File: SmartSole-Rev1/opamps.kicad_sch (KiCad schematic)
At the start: 23 parts, among them U1 MCP6004

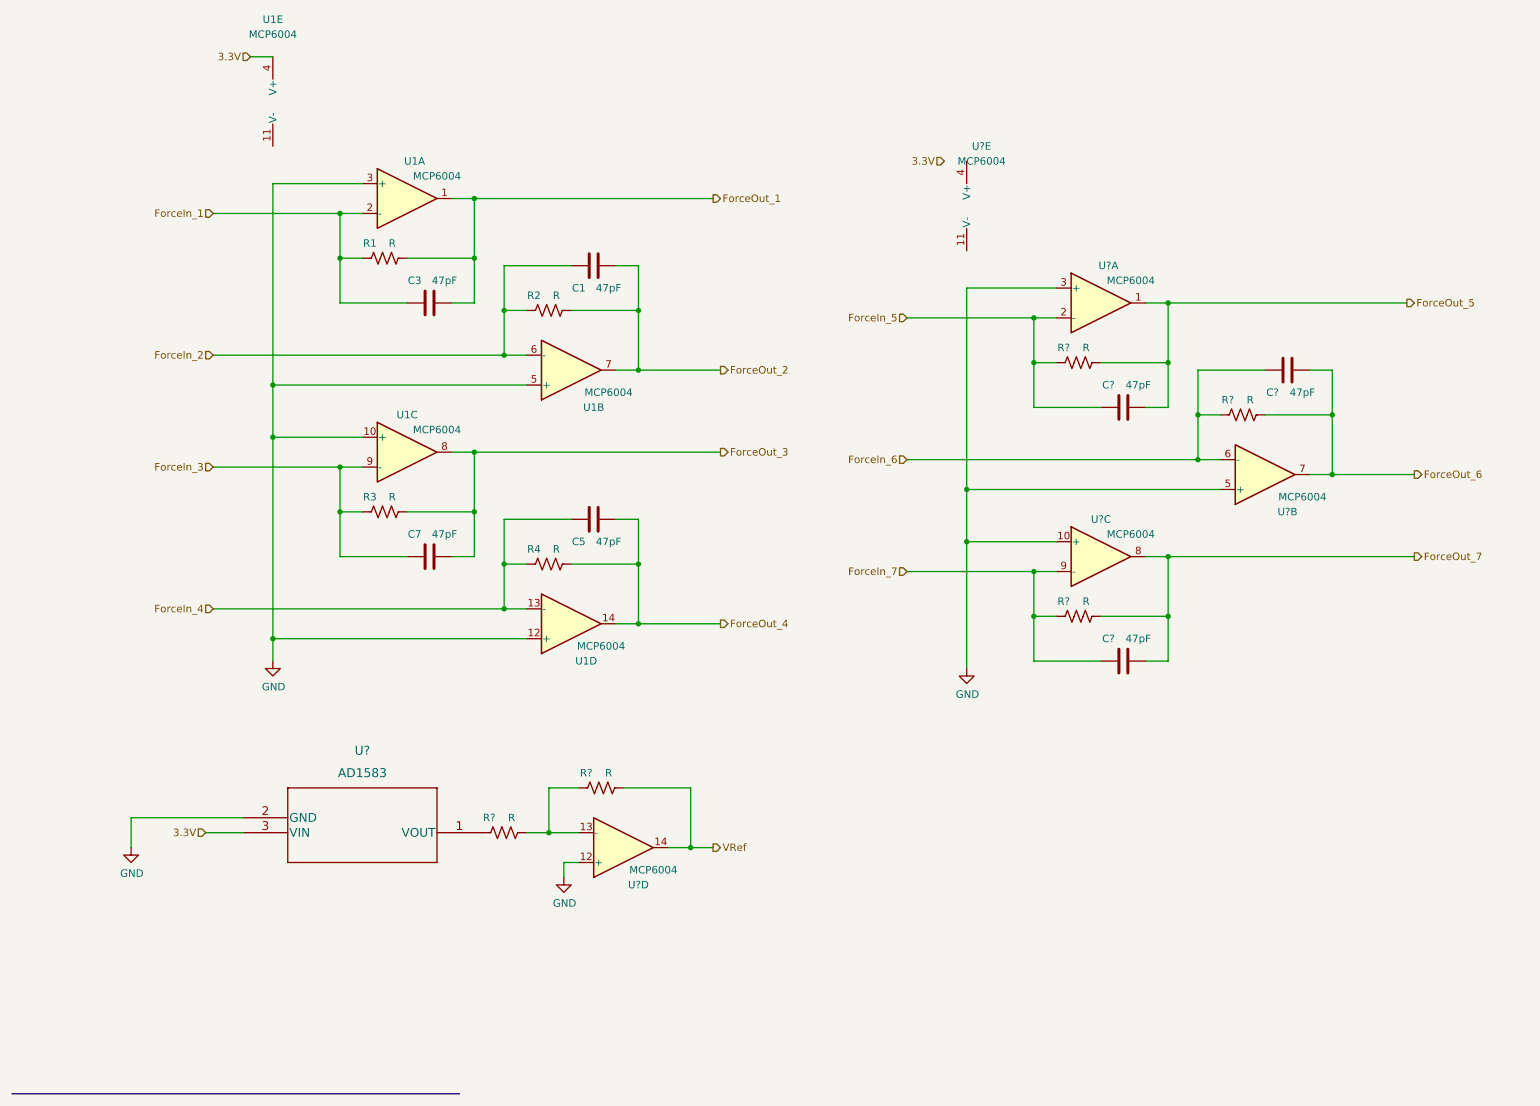
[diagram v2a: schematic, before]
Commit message: Created prelimary board layout, no finalized traces
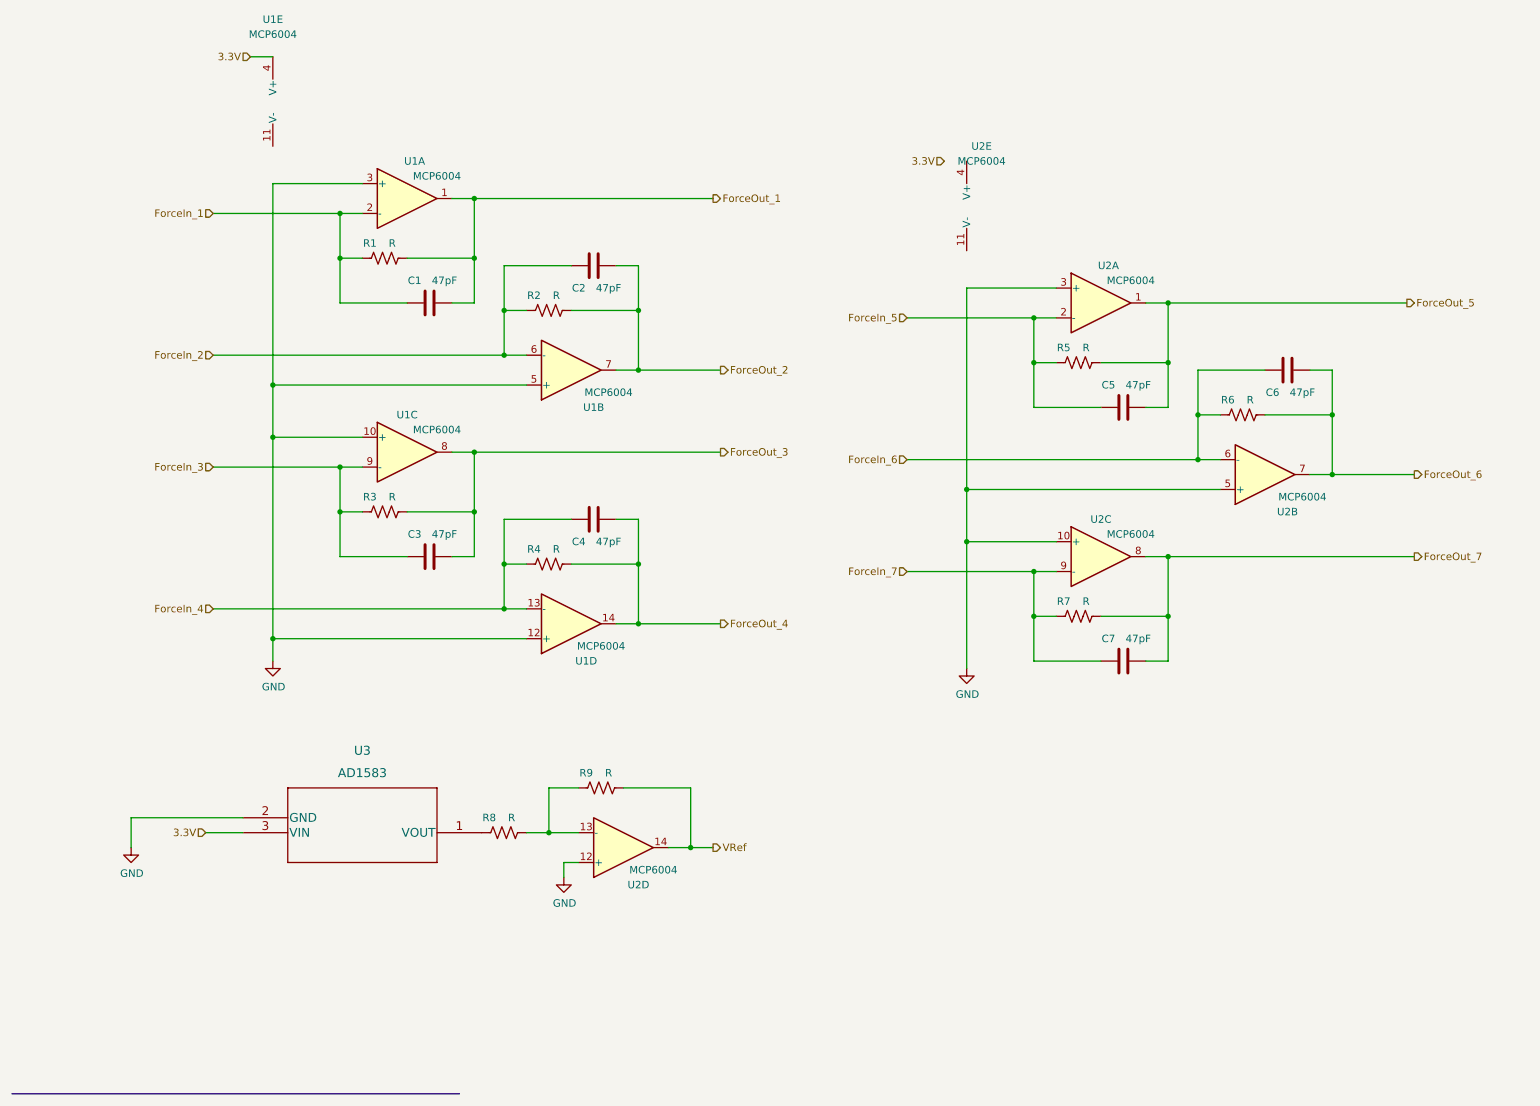
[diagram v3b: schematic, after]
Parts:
- gave numbers to parts that had none: 10
- renumbered C3 to C1, C1 to C2, C7 to C3, C5 to C4
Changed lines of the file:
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@@
   (symbol (lib_id "power:GND") (at 181.61 127 0) (unit 1)
     (in_bom yes) (on_board yes)
-    (property "Reference" "#PWR?" (id 0) (at 181.61 133.35 0)
+    (property "Reference" "#PWR03" (id 0) (at 181.61 133.35 0)
       (effects (font (size 1.27 1.27)) hide)
     )
@@
   (symbol (lib_id "Amplifier_Operational:MCP6004") (at 123.19 157.48 0) (mirror x) (unit 4)
     (in_bom yes) (on_board yes)
-    (property "Reference" "U?" (id 0) (at 125.73 163.83 0))
+    (property "Reference" "U2" (id 0) (at 125.73 163.83 0))
     (property "Value" "MCP6004" (id 1) (at 128.27 161.29 0))
     (property "Footprint" "Package_DIP:DIP-14_W7.62mm" (id 2) (at 121.92 160.02 0)
@@
   (symbol (lib_id "Device:C") (at 90.17 107.95 270) (unit 1)
     (in_bom yes) (on_board yes)
-    (property "Reference" "C7" (id 0) (at 87.63 104.14 90))
+    (property "Reference" "C3" (id 0) (at 87.63 104.14 90))
     (property "Value" "47pF" (id 1) (at 92.71 104.14 90))
     (property "Footprint" "Capacitor_SMD:C_0603_1608Metric" (id 2) (at 86.36 108.9152 0)
@@
   (symbol (lib_id "Device:C") (at 90.17 64.77 270) (unit 1)
     (in_bom yes) (on_board yes)
-    (property "Reference" "C3" (id 0) (at 87.63 60.96 90))
+    (property "Reference" "C1" (id 0) (at 87.63 60.96 90))
     (property "Value" "47pF" (id 1) (at 92.71 60.96 90))
     (property "Footprint" "Capacitor_SMD:C_0603_1608Metric" (id 2) (at 86.36 65.7352 0)
@@
   (symbol (lib_id "Amplifier_Operational:MCP6004") (at 204.47 107.95 0) (unit 3)
     (in_bom yes) (on_board yes)
-    (property "Reference" "U?" (id 0) (at 204.47 101.6 0))
+    (property "Reference" "U2" (id 0) (at 204.47 101.6 0))
     (property "Value" "MCP6004" (id 1) (at 209.55 104.14 0))
     (property "Footprint" "Package_DIP:DIP-14_W7.62mm" (id 2) (at 203.2 105.41 0)
@@
   (symbol (lib_id "Device:C") (at 208.28 82.55 270) (unit 1)
     (in_bom yes) (on_board yes)
-    (property "Reference" "C?" (id 0) (at 205.74 78.74 90))
+    (property "Reference" "C5" (id 0) (at 205.74 78.74 90))
     (property "Value" "47pF" (id 1) (at 210.82 78.74 90))
     (property "Footprint" "Capacitor_SMD:C_0603_1608Metric" (id 2) (at 204.47 83.5152 0)
@@
   (symbol (lib_id "Amplifier_Operational:MCP6004") (at 232.41 93.98 0) (mirror x) (unit 2)
     (in_bom yes) (on_board yes)
-    (property "Reference" "U?" (id 0) (at 236.22 100.33 0))
+    (property "Reference" "U2" (id 0) (at 236.22 100.33 0))
     (property "Value" "MCP6004" (id 1) (at 238.76 97.79 0))
     (property "Footprint" "Package_DIP:DIP-14_W7.62mm" (id 2) (at 231.14 96.52 0)
@@
   (symbol (lib_id "Device:R_US") (at 228.6 83.82 90) (unit 1)
     (in_bom yes) (on_board yes)
-    (property "Reference" "R?" (id 0) (at 226.06 81.28 90))
+    (property "Reference" "R6" (id 0) (at 226.06 81.28 90))
     (property "Value" "R" (id 1) (at 229.87 81.28 90))
     (property "Footprint" "Resistor_SMD:R_0603_1608Metric" (id 2) (at 228.854 82.804 90)
@@
   (symbol (lib_id "Device:R_US") (at 119.38 147.32 90) (unit 1)
     (in_bom yes) (on_board yes)
-    (property "Reference" "R?" (id 0) (at 116.84 144.78 90))
+    (property "Reference" "R9" (id 0) (at 116.84 144.78 90))
     (property "Value" "R" (id 1) (at 120.65 144.78 90))
     (property "Footprint" "Resistor_SMD:R_0603_1608Metric" (id 2) (at 119.634 146.304 90)
@@
   (symbol (lib_id "Device:R_US") (at 200.66 74.93 90) (unit 1)
     (in_bom yes) (on_board yes)
-    (property "Reference" "R?" (id 0) (at 198.12 72.39 90))
+    (property "Reference" "R5" (id 0) (at 198.12 72.39 90))
     (property "Value" "R" (id 1) (at 201.93 72.39 90))
     (property "Footprint" "Resistor_SMD:R_0603_1608Metric" (id 2) (at 200.914 73.914 90)
@@
   (symbol (lib_id "power:GND") (at 39.37 157.48 0) (unit 1)
     (in_bom yes) (on_board yes)
-    (property "Reference" "#PWR?" (id 0) (at 39.37 163.83 0)
+    (property "Reference" "#PWR04" (id 0) (at 39.37 163.83 0)
       (effects (font (size 1.27 1.27)) hide)
     )
@@
   (symbol (lib_id "Device:R_US") (at 200.66 118.11 90) (unit 1)
     (in_bom yes) (on_board yes)
-    (property "Reference" "R?" (id 0) (at 198.12 115.57 90))
+    (property "Reference" "R7" (id 0) (at 198.12 115.57 90))
     (property "Value" "R" (id 1) (at 201.93 115.57 90))
     (property "Footprint" "Resistor_SMD:R_0603_1608Metric" (id 2) (at 200.914 117.094 90)
@@
   (symbol (lib_id "Amplifier_Operational:MCP6004") (at 204.47 64.77 0) (unit 1)
     (in_bom yes) (on_board yes)
-    (property "Reference" "U?" (id 0) (at 205.74 58.42 0))
+    (property "Reference" "U2" (id 0) (at 205.74 58.42 0))
     (property "Value" "MCP6004" (id 1) (at 209.55 60.96 0))
     (property "Footprint" "Package_DIP:DIP-14_W7.62mm" (id 2) (at 203.2 62.23 0)
@@
   (symbol (lib_id "Device:C") (at 118.11 101.6 270) (mirror x) (unit 1)
     (in_bom yes) (on_board yes)
-    (property "Reference" "C5" (id 0) (at 115.57 105.41 90))
+    (property "Reference" "C4" (id 0) (at 115.57 105.41 90))
     (property "Value" "47pF" (id 1) (at 120.65 105.41 90))
     (property "Footprint" "Capacitor_SMD:C_0603_1608Metric" (id 2) (at 114.3 100.6348 0)
@@
   (symbol (lib_id "Device:C") (at 118.11 58.42 270) (mirror x) (unit 1)
     (in_bom yes) (on_board yes)
-    (property "Reference" "C1" (id 0) (at 115.57 62.23 90))
+    (property "Reference" "C2" (id 0) (at 115.57 62.23 90))
     (property "Value" "47pF" (id 1) (at 120.65 62.23 90))
     (property "Footprint" "Capacitor_SMD:C_0603_1608Metric" (id 2) (at 114.3 57.4548 0)
@@
   (symbol (lib_id "Amplifier_Operational:MCP6004") (at 184.15 48.26 0) (unit 5)
     (in_bom yes) (on_board yes) (fields_autoplaced)
-    (property "Reference" "U?" (id 0) (at 184.15 38.1 0))
+    (property "Reference" "U2" (id 0) (at 184.15 38.1 0))
     (property "Value" "MCP6004" (id 1) (at 184.15 40.64 0))
     (property "Footprint" "Package_DIP:DIP-14_W7.62mm" (id 2) (at 182.88 45.72 0)
@@
   (symbol (lib_id "Device:C") (at 236.22 76.2 270) (mirror x) (unit 1)
     (in_bom yes) (on_board yes)
-    (property "Reference" "C?" (id 0) (at 233.68 80.01 90))
+    (property "Reference" "C6" (id 0) (at 233.68 80.01 90))
     (property "Value" "47pF" (id 1) (at 238.76 80.01 90))
     (property "Footprint" "Capacitor_SMD:C_0603_1608Metric" (id 2) (at 232.41 75.2348 0)
@@
   (symbol (lib_id "power:GND") (at 113.03 162.56 0) (unit 1)
     (in_bom yes) (on_board yes)
-    (property "Reference" "#PWR?" (id 0) (at 113.03 168.91 0)
+    (property "Reference" "#PWR05" (id 0) (at 113.03 168.91 0)
       (effects (font (size 1.27 1.27)) hide)
     )
@@
   (symbol (lib_id "CapstoneLibrary:AD1583") (at 99.06 154.94 180) (unit 1)
     (in_bom yes) (on_board yes) (fields_autoplaced)
-    (property "Reference" "U?" (id 0) (at 78.74 140.97 0)
+    (property "Reference" "U3" (id 0) (at 78.74 140.97 0)
       (effects (font (size 1.524 1.524)))
     )
@@
   (symbol (lib_id "Device:C") (at 208.28 125.73 270) (unit 1)
     (in_bom yes) (on_board yes)
-    (property "Reference" "C?" (id 0) (at 205.74 121.92 90))
+    (property "Reference" "C7" (id 0) (at 205.74 121.92 90))
     (property "Value" "47pF" (id 1) (at 210.82 121.92 90))
     (property "Footprint" "Capacitor_SMD:C_0603_1608Metric" (id 2) (at 204.47 126.6952 0)
@@
   (symbol (lib_id "Device:R_US") (at 102.87 154.94 90) (unit 1)
     (in_bom yes) (on_board yes)
-    (property "Reference" "R?" (id 0) (at 100.33 152.4 90))
+    (property "Reference" "R8" (id 0) (at 100.33 152.4 90))
     (property "Value" "R" (id 1) (at 104.14 152.4 90))
     (property "Footprint" "Resistor_SMD:R_0603_1608Metric" (id 2) (at 103.124 153.924 90)

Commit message: First review with rachel, made notes on changes to be made
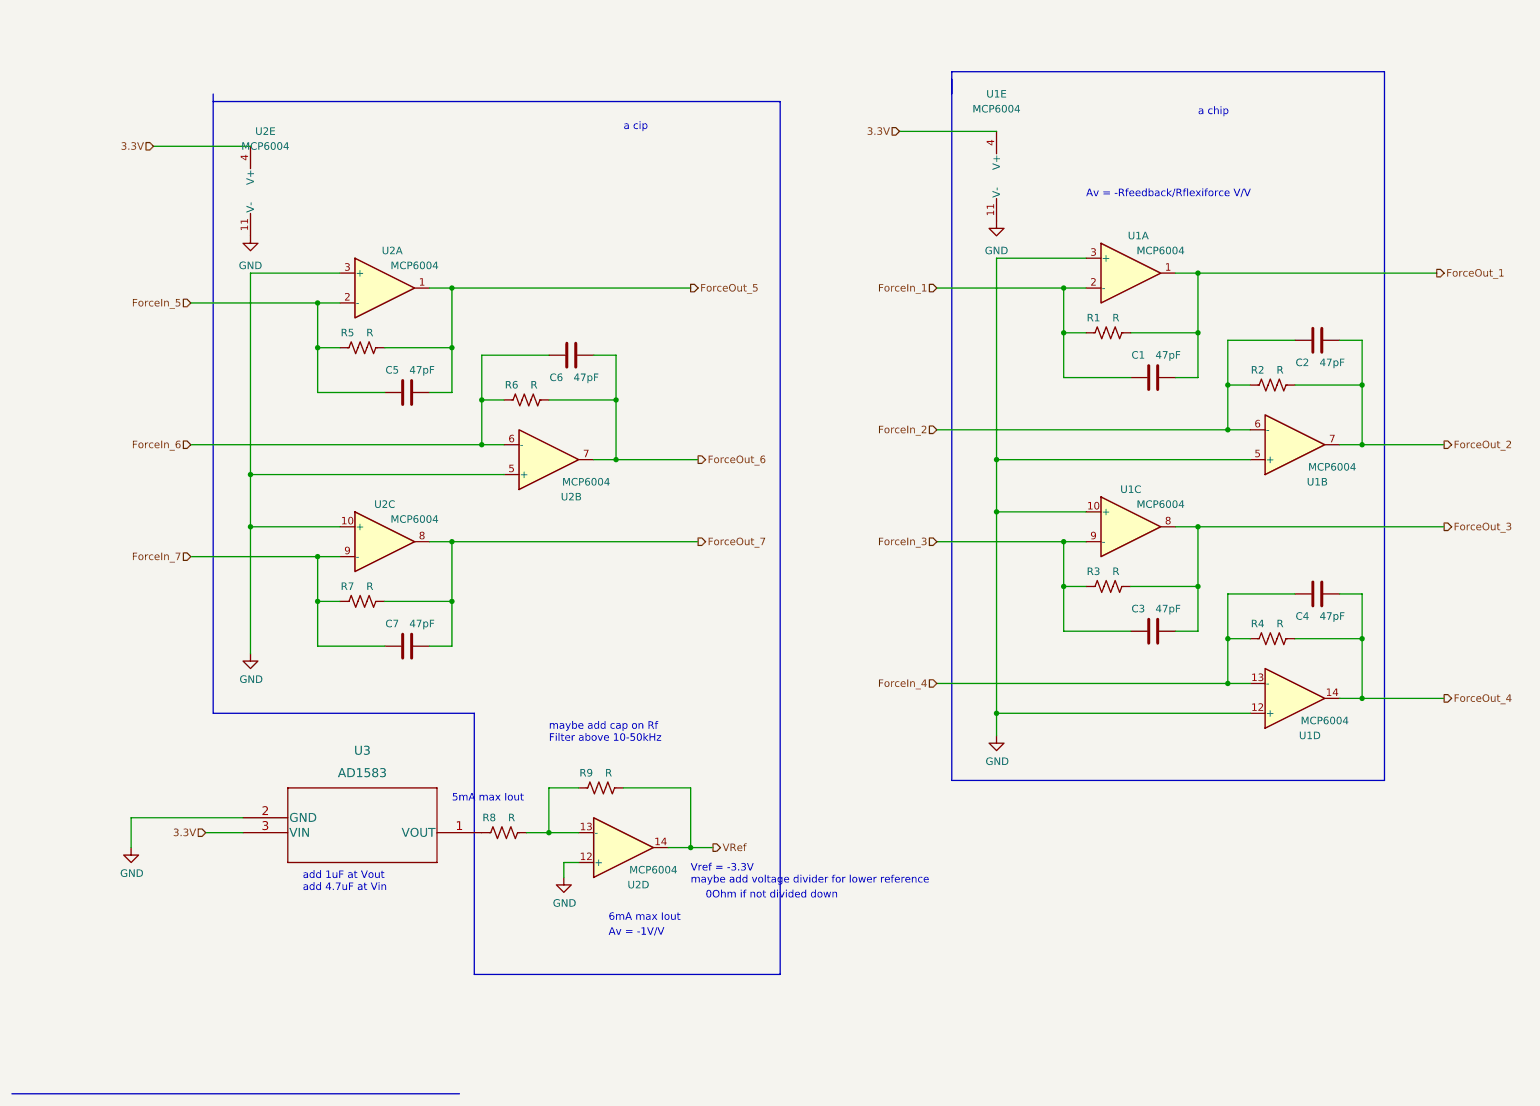
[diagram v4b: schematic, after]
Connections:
- net 3.3V: now also U2.4 (V+)
- net GND: now also U1.11 (V-), U2.11 (V-)
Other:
- note added: "0Ohm if not divided down"
- note added: "5mA max Iout"
- note added: "6mA max Iout"
- note added: "Av = -1V/V"
- note added: "Av = -Rfeedback/Rflexiforce V/V"
- note added: "Vref = -3.3V maybe add voltage divider for lower reference"
- note added: "a chip"
- note added: "a cip"
- note added: "add 1uF at Vout add 4.7uF at Vin"
- note added: "maybe add cap on Rf Filter above 10-50kHz"
- moved on the sheet: C1, C2, C3, C4, C5, C6, C7, R1, R2, R3, R4, R5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
